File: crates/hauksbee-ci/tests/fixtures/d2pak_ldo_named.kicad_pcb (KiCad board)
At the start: 3 parts, among them U1 LD1086D2T33TR

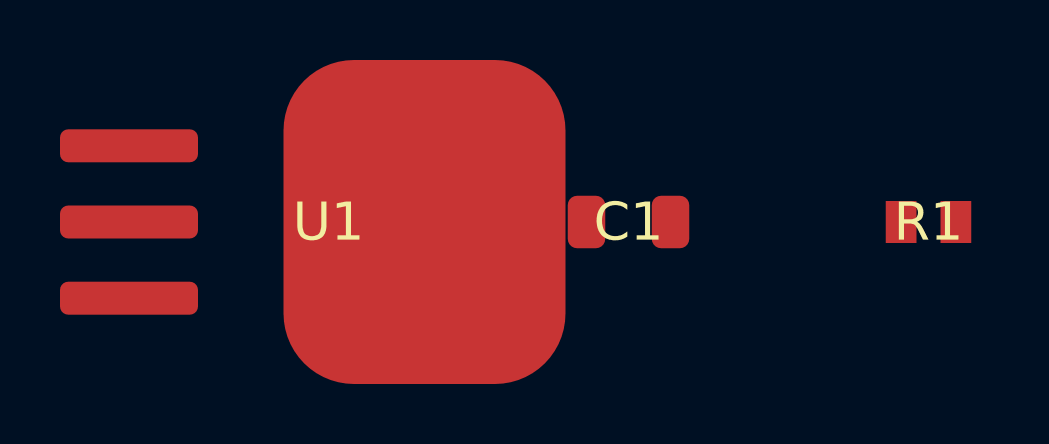
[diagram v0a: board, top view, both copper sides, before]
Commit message: Static-gate fallout: physical fixtures, true findings kept, two false alarms fixed by invariant
The CI run fails on every finding that gates `hauksbee check`. The fixtures
and tests that broke under that rule now follow it, and none of them hide it.

- Synthetic fixtures are physically valid: pads are spaced and copper is
 routed where a board must check clean. The d2pak and adj-regulator boards
 use 1210 resistors, and the comparator board has its J1 supply.
- Board-as-Code fixtures can't carry copper. Each one has a visible
 [[waive]] for unrouted_pad with a reason, and its test asserts that the
 waived row is still listed.
- The tolerance_divider example board routes VOUT, so blinky-permissive and
 the divider examples no longer fail on "not routed".
- True findings keep their rows, and the expectations now say so:
 - Tarski unlimited_base_drive: the BCM847BS base is driven from the
 LVC1G3157 B2/A channel through rON only.
 - Tarski cap_no_dc_path: the 1N4148 reverse leakage is bounded only from
 above.
 The repaired flagship and neuron examples are RED only on those rows, and
 the docs are updated to match.
- Strap lint (false alarm, Olimex rev L): a carded voltage detector that
 holds the oscillator enable low counts as following the MCU reset when its
 sense node is fed only by:
 - resistors from the reset net
 - capacitors to ground
 - discharge-only diode anodes, read from the diode card
 This is decided from topology and cards, not from net names. It adds a
 legal control and a faulty control.
- power_pin_wiring (false alarm, CP2104 VIO tied to VDD): the new
 optional_supplies.regulated_from field says the pin is an on-chip
 regulator's output. When that regulator's input is fed, the pin feeds the
 part's other supplies.
 - CP2102 and CP2104 gain this field.
 - MAX17760 VCC is an optional (LDO output) supply.
 - The datasheet basis is cited in each card.
- The CI static gate reports waived rows separately, and a measurement-only
 run beside a waived row st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
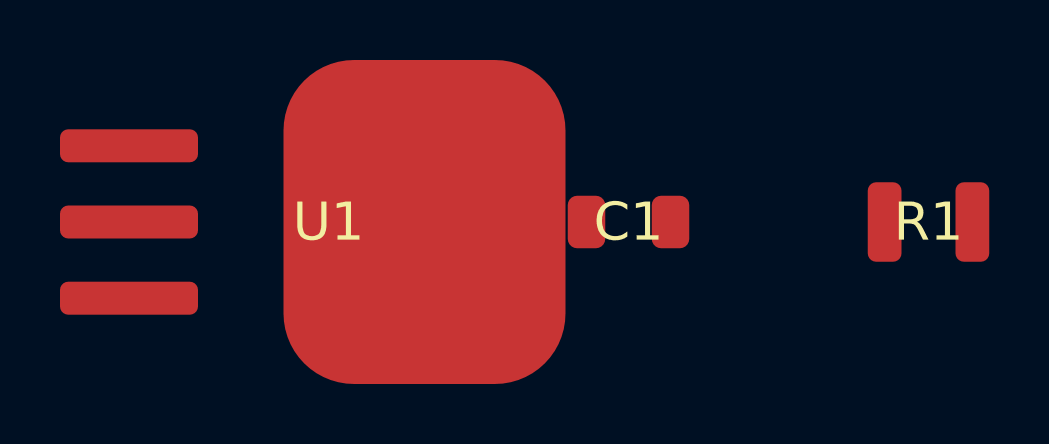
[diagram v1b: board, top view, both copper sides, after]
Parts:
- R1: footprint Resistor_SMD:R_0805_2012Metric -> Resistor_SMD:R_1210_3225Metric
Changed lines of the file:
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@@
     (pad "2" smd roundrect (at 1.4 0) (size 1.25 1.75) (layers "F.Cu" "F.Paste" "F.Mask") (net 1 "GND"))
   )
-  (footprint "Resistor_SMD:R_0805_2012Metric" (layer "F.Cu")
+  (footprint "Resistor_SMD:R_1210_3225Metric" (layer "F.Cu")
     (at 40 20)
     (property "Reference" "R1" (at 0 0) (layer "F.SilkS"))
     (property "Value" "33" (at 0 2) (layer "F.Fab"))
-    (pad "1" smd rect (at -0.9125 0) (size 1.025 1.4) (layers "F.Cu" "F.Paste" "F.Mask") (net 3 "VOUT"))
-    (pad "2" smd rect (at 0.9125 0) (size 1.025 1.4) (layers "F.Cu" "F.Paste" "F.Mask") (net 1 "GND"))
+    (pad "1" smd roundrect (at -1.4625 0) (size 1.125 2.65) (layers "F.Cu" "F.Paste" "F.Mask") (net 3 "VOUT"))
+    (pad "2" smd roundrect (at 1.4625 0) (size 1.125 2.65) (layers "F.Cu" "F.Paste" "F.Mask") (net 1 "GND"))
   )
 )
